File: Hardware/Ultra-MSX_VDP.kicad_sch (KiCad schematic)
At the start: 4 parts, among them J3 Ultra-VDP-daughter

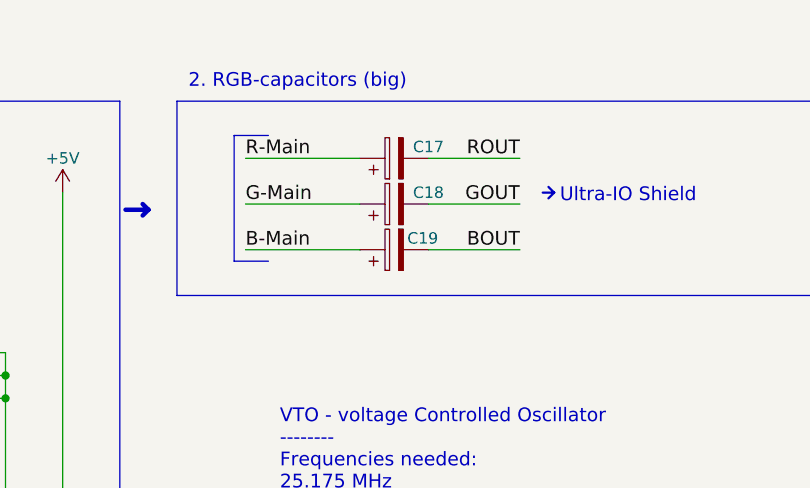
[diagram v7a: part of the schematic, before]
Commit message: Added cooler and CPU-mount footprints, as well as Indication LEDs.
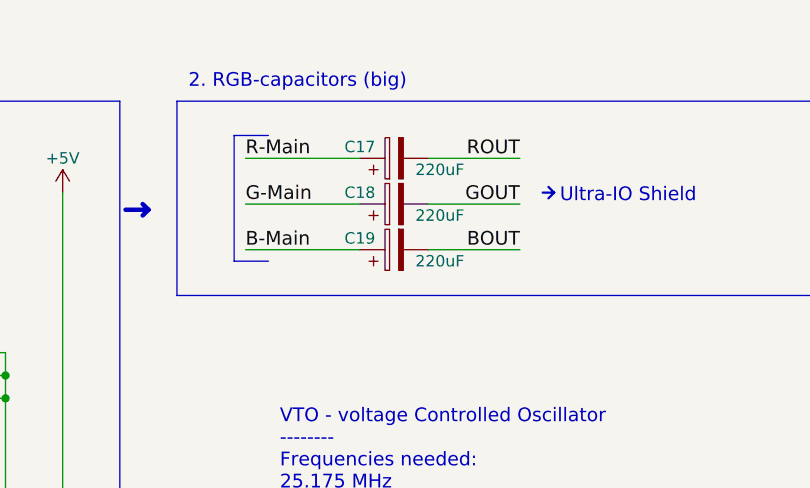
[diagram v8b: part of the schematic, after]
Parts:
- C17, C18, C19: value C_Polarized -> C_TCJB227; footprint Ultra-MSX:Cap_Elec_Radial_10mm -> Capacitor_Tantalum_SMD:CP_EIA-3528-15_AVX-H; symbol Device:C_Polarized -> LRJ-parts:C_TCJB227; Capacitance (none) -> 220uF; MPN (none) -> TCJB227M006R0070; Manufacturer (none) -> KYOCERA AVX; Voltage Rating (none) -> 6.3V
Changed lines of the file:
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@@
     (effects (font (size 1.524 1.524)) (justify left))
   )
-  (symbol (lib_id "Device:C_Polarized") (at 124.46 31.75 90) (unit 1)
+  (symbol (lib_id "LRJ-parts:C_TCJB227") (at 124.46 31.75 90) (unit 1)
     (in_bom yes) (on_board yes)
-    (property "Reference" "C18" (id 0) (at 128.27 30.48 90))
-    (property "Value" "C_Polarized" (id 1) (at 130.81 33.02 90)
+    (property "Reference" "C18" (id 0) (at 120.65 30.48 90))
+    (property "Value" "C_TCJB227" (id 1) (at 127 31.115 0)
+      (effects (font (size 1.27 1.27)) (justify left) hide)
+    )
+    (property "Footprint" "Capacitor_Tantalum_SMD:CP_EIA-3528-15_AVX-H" (id 2) (at 128.27 30.7848 0)
       (effects (font (size 1.27 1.27)) hide)
     )
-    (property "Footprint" "Ultra-MSX:Cap_Elec_Radial_10mm" (id 2) (at 128.27 30.7848 0)
+    (property "Datasheet" "https://datasheets.kyocera-avx.com/TCJ.pdf" (id 3) (at 129.54 6.35 0)
       (effects (font (size 1.27 1.27)) hide)
     )
-    (property "Datasheet" "~" (id 3) (at 124.46 31.75 0)
+    (property "MPN" "TCJB227M006R0070" (id 4) (at 121.92 16.51 0)
       (effects (font (size 1.27 1.27)) hide)
     )
+    (property "Voltage Rating" "6.3V" (id 5) (at 124.46 24.13 0)
+      (effects (font (size 1.27 1.27)) hide)
+    )
+    (property "Manufacturer" "KYOCERA AVX" (id 6) (at 119.38 19.05 0)
+      (effects (font (size 1.27 1.27)) hide)
+    )
+    (property "Capacitance" "220uF" (id 7) (at 129.54 33.02 90))
     (pin "1")
     (pin "2")
@@
     (pin "1")
   )
-  (symbol (lib_id "Device:C_Polarized") (at 124.46 26.67 90) (unit 1)
+  (symbol (lib_id "LRJ-parts:C_TCJB227") (at 124.46 26.67 90) (unit 1)
     (in_bom yes) (on_board yes)
-    (property "Reference" "C17" (id 0) (at 128.27 25.4 90))
-    (property "Value" "C_Polarized" (id 1) (at 124.46 22.86 90)
+    (property "Reference" "C17" (id 0) (at 120.65 25.4 90))
+    (property "Value" "C_TCJB227" (id 1) (at 127 26.035 0)
+      (effects (font (size 1.27 1.27)) (justify left) hide)
+    )
+    (property "Footprint" "Capacitor_Tantalum_SMD:CP_EIA-3528-15_AVX-H" (id 2) (at 128.27 25.7048 0)
       (effects (font (size 1.27 1.27)) hide)
     )
-    (property "Footprint" "Ultra-MSX:Cap_Elec_Radial_10mm" (id 2) (at 128.27 25.7048 0)
+    (property "Datasheet" "https://datasheets.kyocera-avx.com/TCJ.pdf" (id 3) (at 129.54 1.27 0)
       (effects (font (size 1.27 1.27)) hide)
     )
-    (property "Datasheet" "~" (id 3) (at 124.46 26.67 0)
+    (property "MPN" "TCJB227M006R0070" (id 4) (at 121.92 11.43 0)
       (effects (font (size 1.27 1.27)) hide)
     )
+    (property "Voltage Rating" "6.3V" (id 5) (at 124.46 19.05 0)
+      (effects (font (size 1.27 1.27)) hide)
+    )
+    (property "Manufacturer" "KYOCERA AVX" (id 6) (at 119.38 13.97 0)
+      (effects (font (size 1.27 1.27)) hide)
+    )
+    (property "Capacitance" "220uF" (id 7) (at 129.54 27.94 90))
     (pin "1")
     (pin "2")
@@
     (pin "1")
   )
-  (symbol (lib_id "Device:C_Polarized") (at 124.46 36.83 90) (unit 1)
+  (symbol (lib_id "LRJ-parts:C_TCJB227") (at 124.46 36.83 90) (unit 1)
     (in_bom yes) (on_board yes)
-    (property "Reference" "C19" (id 0) (at 127.635 35.56 90))
-    (property "Value" "C_Polarized" (id 1) (at 124.46 40.64 90)
+    (property "Reference" "C19" (id 0) (at 120.65 35.56 90))
+    (property "Value" "C_TCJB227" (id 1) (at 127 36.195 0)
+      (effects (font (size 1.27 1.27)) (justify left) hide)
+    )
+    (property "Footprint" "Capacitor_Tantalum_SMD:CP_EIA-3528-15_AVX-H" (id 2) (at 128.27 35.8648 0)
       (effects (font (size 1.27 1.27)) hide)
     )
-    (property "Footprint" "Ultra-MSX:Cap_Elec_Radial_10mm" (id 2) (at 128.27 35.8648 0)
+    (property "Datasheet" "https://datasheets.kyocera-avx.com/TCJ.pdf" (id 3) (at 129.54 11.43 0)
       (effects (font (size 1.27 1.27)) hide)
     )
-    (property "Datasheet" "~" (id 3) (at 124.46 36.83 0)
+    (property "MPN" "TCJB227M006R0070" (id 4) (at 121.92 21.59 0)
       (effects (font (size 1.27 1.27)) hide)
     )
+    (property "Voltage Rating" "6.3V" (id 5) (at 124.46 29.21 0)
+      (effects (font (size 1.27 1.27)) hide)
+    )
+    (property "Manufacturer" "KYOCERA AVX" (id 6) (at 119.38 24.13 0)
+      (effects (font (size 1.27 1.27)) hide)
+    )
+    (property "Capacitance" "220uF" (id 7) (at 129.54 38.1 90))
     (pin "1")
     (pin "2")
